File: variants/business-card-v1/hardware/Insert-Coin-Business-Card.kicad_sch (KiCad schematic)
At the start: 49 parts, among them J1 Conn_01x02, Q1 CJ3400, Q10 CJ3400, Q2 CJ3400, Q3 CJ3400, Q4 CJ3400, Q5 CJ3400, Q7 CJ3400, Q8 CJ3400, Q9 CJ3400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

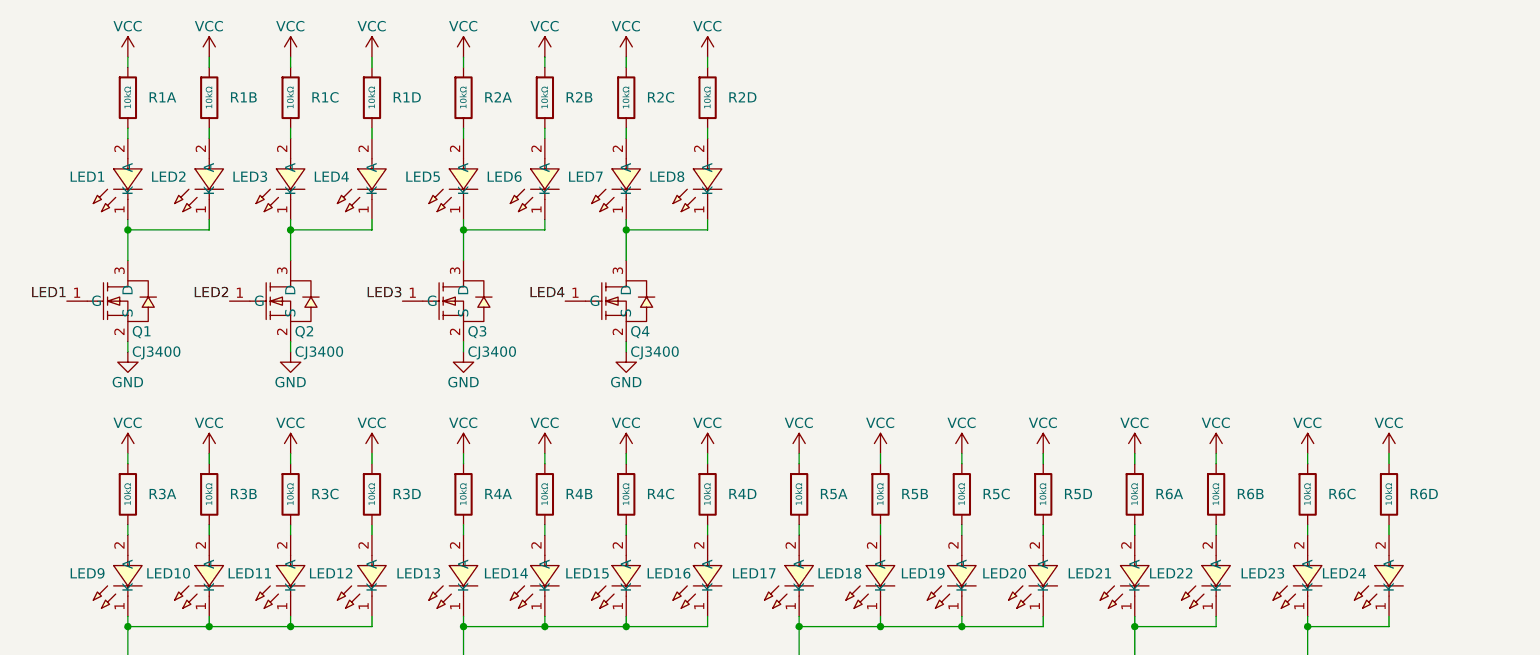
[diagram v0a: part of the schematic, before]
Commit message: default to production & Kicad Resistor fix
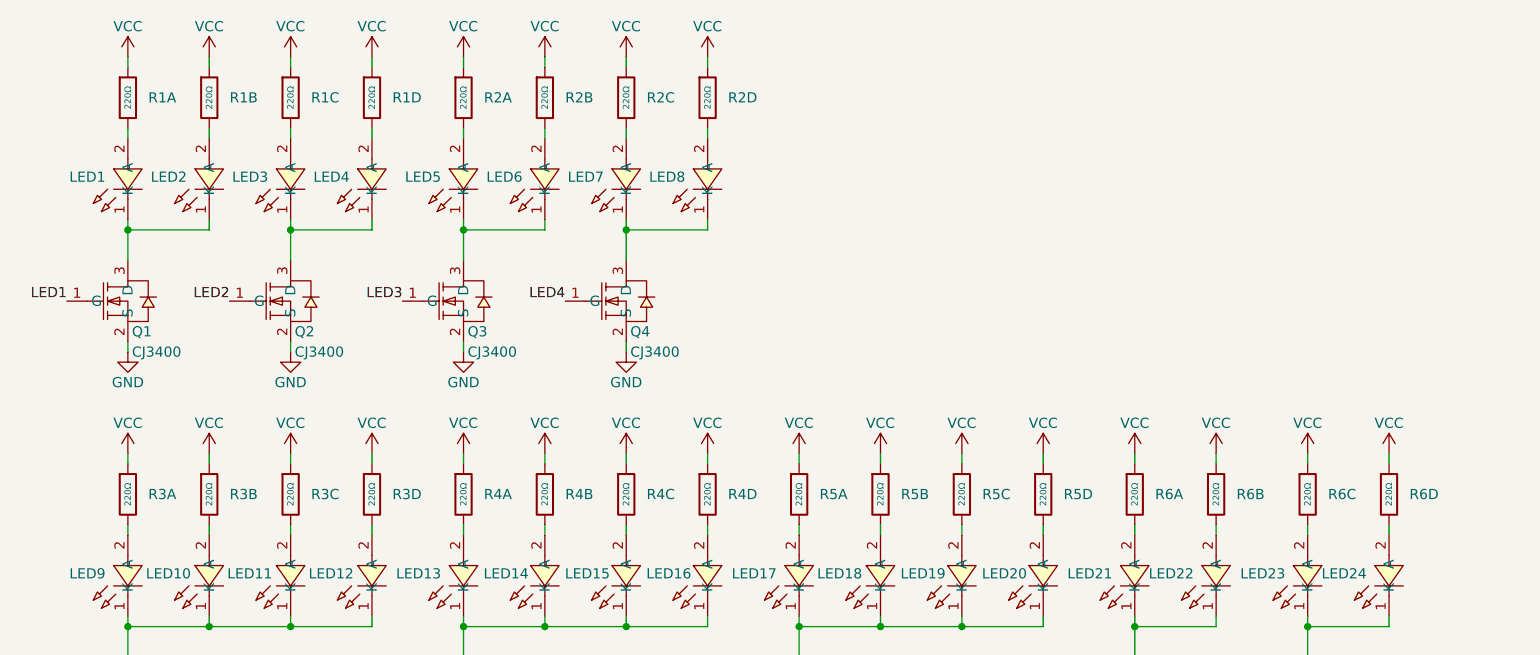
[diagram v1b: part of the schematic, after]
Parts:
- R1, R2, R3, R4, R5, R6: value 10kΩ -> 220Ω; LCSC C25725 -> C25498; Resistance 10kΩ -> 220Ω; Stock 62997 -> (none); Temperature Coefficient ±200ppm/°C -> (none); Tolerance ±5% -> (none)
